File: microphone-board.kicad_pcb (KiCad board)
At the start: 4 copper layers, 10.7 x 11 mm, 13 parts, among them J1 Conn_FFC_Molex_5019510550

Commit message: [#72278] Route connections
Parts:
- removed D3: TPD1E0B04_XDFN-2, antmicro-footprints:XDFN-2_1x0.60mm
- MK1: value MK_SPH0645LM4H-B -> MK_SPH0644LM4H-1; footprint antmicro-footprints:MK_SPH0645LM4H-B -> antmicro-footprints:MK_SPH0644LM4H-1
- moved D4 2.18 mm to (242.1, 146.3), turned to 0 degrees
- moved MK1 0.88 mm to (240.0, 145.0)
- moved R1 0.28 mm to (240.1, 142.4)
- moved R3 0.08 mm to (237.7, 143.2)
- moved C1 0.06 mm to (242.4, 143.7)
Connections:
- net /BCLK renamed /CLK
- J1 pad 4: /WS -> GND
- MK1 pad 1: /WS -> Net-(MK1-DATA)
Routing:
- net /WS: track 8.01 -> 0.00 mm, vias 2 -> 0
- net /CLK: track 8.91 -> 12.6 mm
- net /DATA: track 12.5 -> 9.08 mm
- net /SELECT: track 3.85 -> 2.69 mm, vias 2 -> 0
- net GND: track 0.62 -> 0.10 mm, vias 17 -> 18

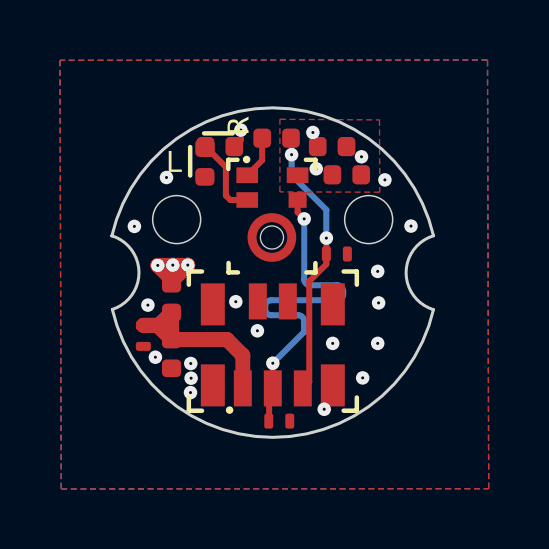
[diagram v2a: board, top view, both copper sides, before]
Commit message: [#72278] Improve power planes
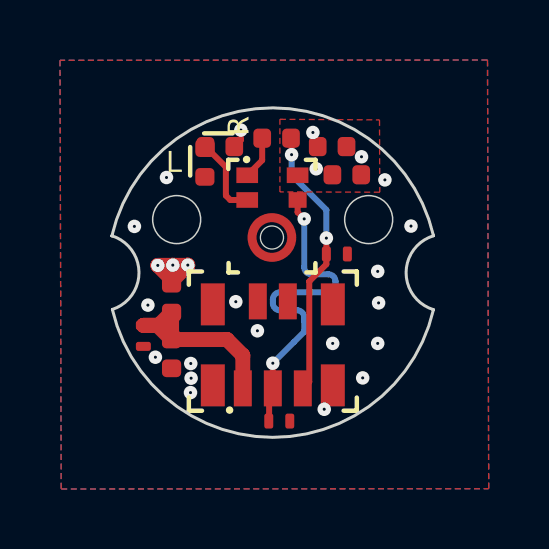
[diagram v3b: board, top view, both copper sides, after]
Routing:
- net /CLK: track 12.6 -> 11.5 mm
- added copper zone on In1.Cu, net VDD
- removed copper zone on In2.Cu, net VDD
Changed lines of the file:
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@@
 	(paper "A3")
 	(title_block
-		(title "Microphone board")
+		(title "Microphone Board")
 		(date "2025-01-29")
 		(rev "1.3.0")
@@
 	)
 	(segment
-		(start 242.1262 147.838045)
-		(end 241.2262 147.838045)
+		(start 240.22213 148.173012)
+		(end 240.7862 148.173012)
 		(width 0.2)
 		(layer "B.Cu")
@@
 	)
 	(segment
-		(start 241.0262 148.638045)
-		(end 241.0262 148.713831)
+		(start 241.0262 148.413012)
+		(end 241.0262 148.533012)
 		(width 0.2)
 		(layer "B.Cu")
@@
 	)
 	(segment
-		(start 242.3262 147.538045)
-		(end 242.3262 147.638045)
+		(start 241.2662 147.573012)
+		(end 240.22213 147.573012)
 		(width 0.2)
 		(layer "B.Cu")
@@
 	)
 	(segment
-		(start 241.026385 145.126483)
-		(end 241.0262 145.126668)
+		(start 239.98213 147.813012)
+		(end 239.98213 147.933012)
 		(width 0.2)
 		(layer "B.Cu")
@@
 	)
 	(segment
-		(start 241.2262 147.338045)
-		(end 242.1262 147.338045)
+		(start 241.026385 145.126483)
+		(end 241.0262 145.126668)
 		(width 0.2)
 		(layer "B.Cu")
@@
 	)
 	(segment
-		(start 239.7262 148.038045)
-		(end 239.7262 148.138045)
+		(start 241.0262 148.8904)
+		(end 240.691033 149.225567)
 		(width 0.2)
 		(layer "B.Cu")
@@
 	)
 	(segment
-		(start 241.0262 148.8904)
+		(start 240.691033 149.225567)
 		(end 239.98 149.9366)
 		(width 0.2)
@@
 	)
 	(segment
-		(start 241.0262 148.538045)
-		(end 241.0262 148.638045)
+		(start 241.2662 146.973012)
+		(end 241.830255 146.973012)
 		(width 0.2)
 		(layer "B.Cu")
@@
 	)
 	(segment
-		(start 241.0262 148.713831)
-		(end 241.0262 148.8904)
+		(start 241.0262 145.126668)
+		(end 241.0262 146.733012)
 		(width 0.2)
 		(layer "B.Cu")
@@
 	)
 	(segment
-		(start 241.0262 145.126668)
-		(end 241.0262 147.138045)
+		(start 242.070255 147.213012)
+		(end 242.070255 147.333012)
 		(width 0.2)
 		(layer "B.Cu")
@@
 	)
 	(segment
-		(start 241.2262 147.838045)
-		(end 239.9262 147.838045)
+		(start 241.0262 148.533012)
+		(end 241.0262 148.8904)
 		(width 0.2)
 		(layer "B.Cu")
@@
 	)
 	(segment
-		(start 239.9262 148.338045)
-		(end 240.8262 148.338045)
+		(start 241.830255 147.573012)
+		(end 241.2662 147.573012)
 		(width 0.2)
 		(layer "B.Cu")
@@
 	)
 	(arc
-		(start 242.1262 147.338045)
-		(mid 242.267621 147.396624)
-		(end 242.3262 147.538045)
+		(start 241.830255 146.973012)
+		(mid 241.999961 147.043306)
+		(end 242.070255 147.213012)
 		(width 0.2)
 		(layer "B.Cu")
@@
 	)
 	(arc
-		(start 239.7262 148.138045)
-		(mid 239.784779 148.279466)
-		(end 239.9262 148.338045)
+		(start 239.98213 147.933012)
+		(mid 240.052424 148.102718)
+		(end 240.22213 148.173012)
 		(width 0.2)
 		(layer "B.Cu")
@@
 	)
 	(arc
-		(start 242.3262 147.638045)
-		(mid 242.267621 147.779466)
-		(end 242.1262 147.838045)
+		(start 240.22213 147.573012)
+		(mid 240.052424 147.643306)
+		(end 239.98213 147.813012)
 		(width 0.2)
 		(layer "B.Cu")
@@
 	)
 	(arc
-		(start 241.0262 147.138045)
-		(mid 241.084779 147.279466)
-		(end 241.2262 147.338045)
+		(start 240.7862 148.173012)
+		(mid 240.955906 148.243306)
+		(end 241.0262 148.413012)
 		(width 0.2)
 		(layer "B.Cu")
@@
 	)
 	(arc
-		(start 239.9262 147.838045)
-		(mid 239.784779 147.896624)
-		(end 239.7262 148.038045)
+		(start 242.070255 147.333012)
+		(mid 241.999961 147.502718)
+		(end 241.830255 147.573012)
 		(width 0.2)
 		(layer "B.Cu")
@@
 	)
 	(arc
-		(start 240.8262 148.338045)
-		(mid 240.967621 148.396624)
-		(end 241.0262 148.538045)
+		(start 241.0262 146.733012)
+		(mid 241.096494 146.902718)
+		(end 241.2662 146.973012)
 		(width 0.2)
 		(layer "B.Cu")
@@
 		(net 1)
 		(net_name "VDD")
-		(layer "In2.Cu")
+		(layer "In1.Cu")
 		(hatch edge 0.5)
 		(priority 1)
@@
 		(polygon
 			(pts
-				(xy 238.2362 141.1566) (xy 238.2162 144.2666) (xy 235.125108 147.007305) (xy 242.2562 146.9666)
-				(xy 242.2562 141.2366)
+				(xy 238.4762 141.4266) (xy 238.4762 144.2666) (xy 234.9762 146.9266) (xy 239.9762 146.9266) (xy 241.9762 144.9266)
+				(xy 241.9762 141.4266)
 			)
 		)
@@
 		(base_line
 			(pts
-				(xy 241.0262 147.138045) (xy 241.0262 148.713831)
+				(xy 241.0262 146.733012) (xy 241.0262 148.8904) (xy 240.691033 149.225567)
 			)
 		)
 		(corner_radius_percent 80)
 		(end
-			(xy 241.0262 148.713831)
+			(xy 240.691033 149.225567)
 		)
 		(initial_side "left")
@@
 		(last_status "tuned")
 		(last_track_width 0.2)
-		(last_tuning "14.5778 mm (tuned)")
-		(max_amplitude 1.3)
+		(last_tuning "13.4512 mm (tuned)")
+		(max_amplitude 1.2)
 		(min_amplitude 0.2)
-		(min_spacing 0.5)
+		(min_spacing 0.6)
 		(origin
-			(xy 241.0262 147.138045)
+			(xy 241.0262 146.733012)
 		)
 		(override_custom_rules no)
 		(rounded yes)
 		(single_sided no)
-		(target_length 1000000)
-		(target_length_max 1000000)
-		(target_length_min 0)
+		(target_length 13.4512)
+		(target_length_max 13.5512)
+		(target_length_min 13.3512)
 		(target_skew 0)
 		(target_skew_max 0.1)
 		(target_skew_min -0.1)
 		(tuning_mode "single")
-		(members 21fd26ad-4f97-41b3-82cd-1ce6f6153cbf 2296c13e-1d2d-4f92-a750-f96d8d1c2f30
-			5bb8a710-dbc9-422e-9839-212e2c8cd6e3 8b89ae5a-5055-41cd-b712-40c804e0e177
-			955825f6-63c6-40ef-b245-055c87beeccd 9af8b386-e426-43e1-b3d8-8812363dade3
-			a293b5e8-b0fc-4a59-bcdb-991cd90658ec ac802156-9d82-4d42-b423-83698214e503
-			b29cf54f-2439-4eff-9f75-ccb173cda50a c8115202-0245-444a-9e00-17e41dcfae32
-			c862495f-9cc7-489a-8fa7-afc298645df3 ceeb5a3a-a95a-418c-8e67-a7ccacfeae25
-			de13743b-db5a-4380-a661-417c874c5d1d f2508ada-b89c-470e-bafd-2dc4f7dc9fe5
+		(members 0dc3342d-397f-4a9e-be53-1496eb094c93 1a89527e-9d41-4e57-be6f-a60174c1f229
+			1af9c8fd-b58c-4abc-969b-1e065412c01e 3d1da326-2633-4911-a51f-2d8ad4816fc0
+			4398ac31-fd37-4aef-827e-6fba7f7ce36d 5f208083-7cf9-4310-9dd2-3c2c89777015
+			68a24e4c-6378-4d9a-8719-ca68d13f032a 6ce442df-b7d0-43e0-b9f0-db657edfb739
+			a390a7a3-a116-499c-819e-6a47caa2658c ba152155-d876-4163-96ce-08605484f5fe
+			bdb553d2-9e70-4875-bc4a-806de15caff5 d54d2238-1250-484f-bf60-89a839bb12cf
+			d627c6ad-4c15-4112-8c83-9000af08f0f1 ec613cfb-3b53-436a-b0fb-c2baaaa50088
+			fb2c88a3-1405-413f-aa07-2e49fc72c722
 		)
 	)
